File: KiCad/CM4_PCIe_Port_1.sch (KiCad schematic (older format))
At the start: 3 parts, among them J14 PCIe_x16

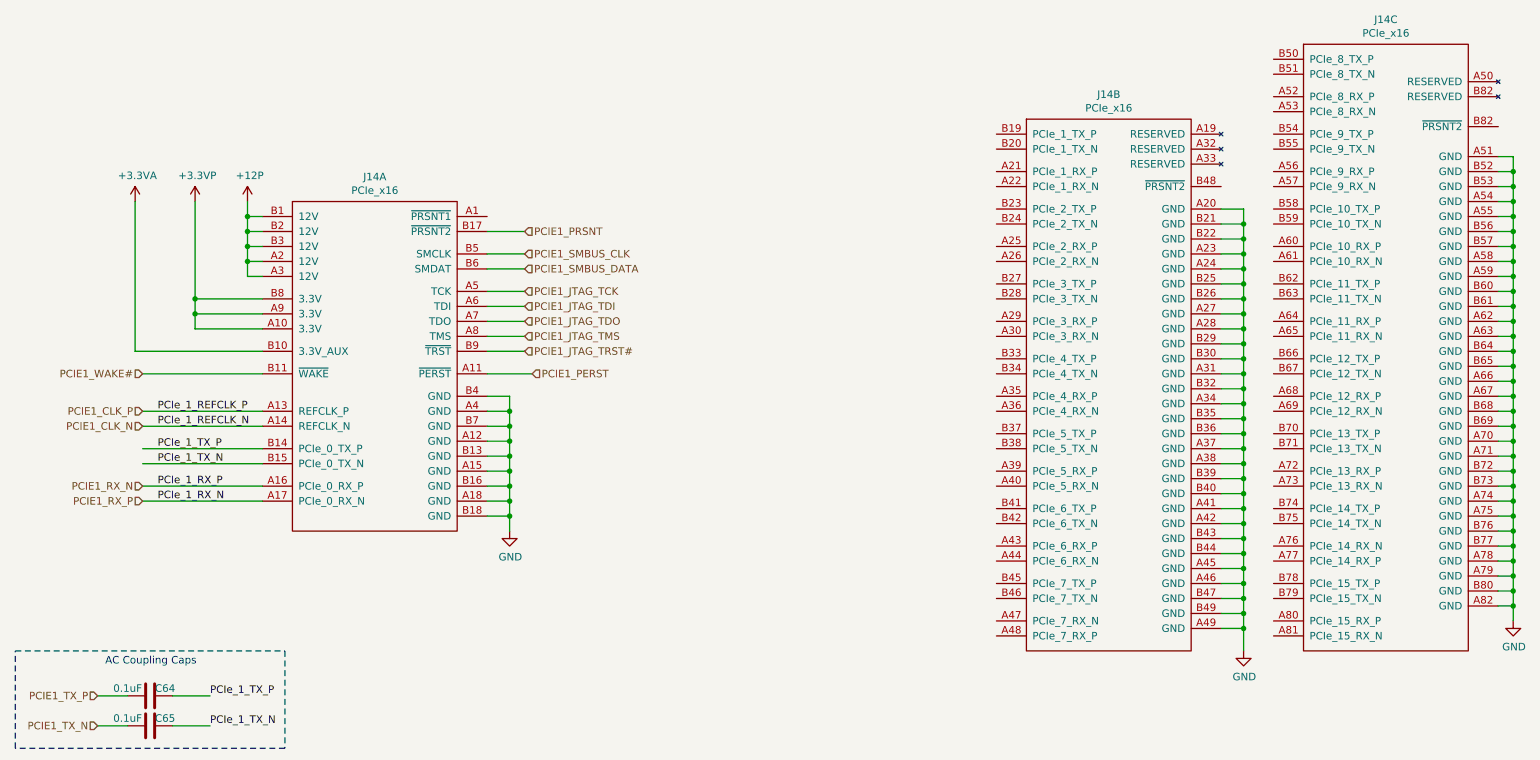
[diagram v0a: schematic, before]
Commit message: Tons of wiring and pin straps for PCI-e Switch
Also re-did some hierarchical labels for JTAG
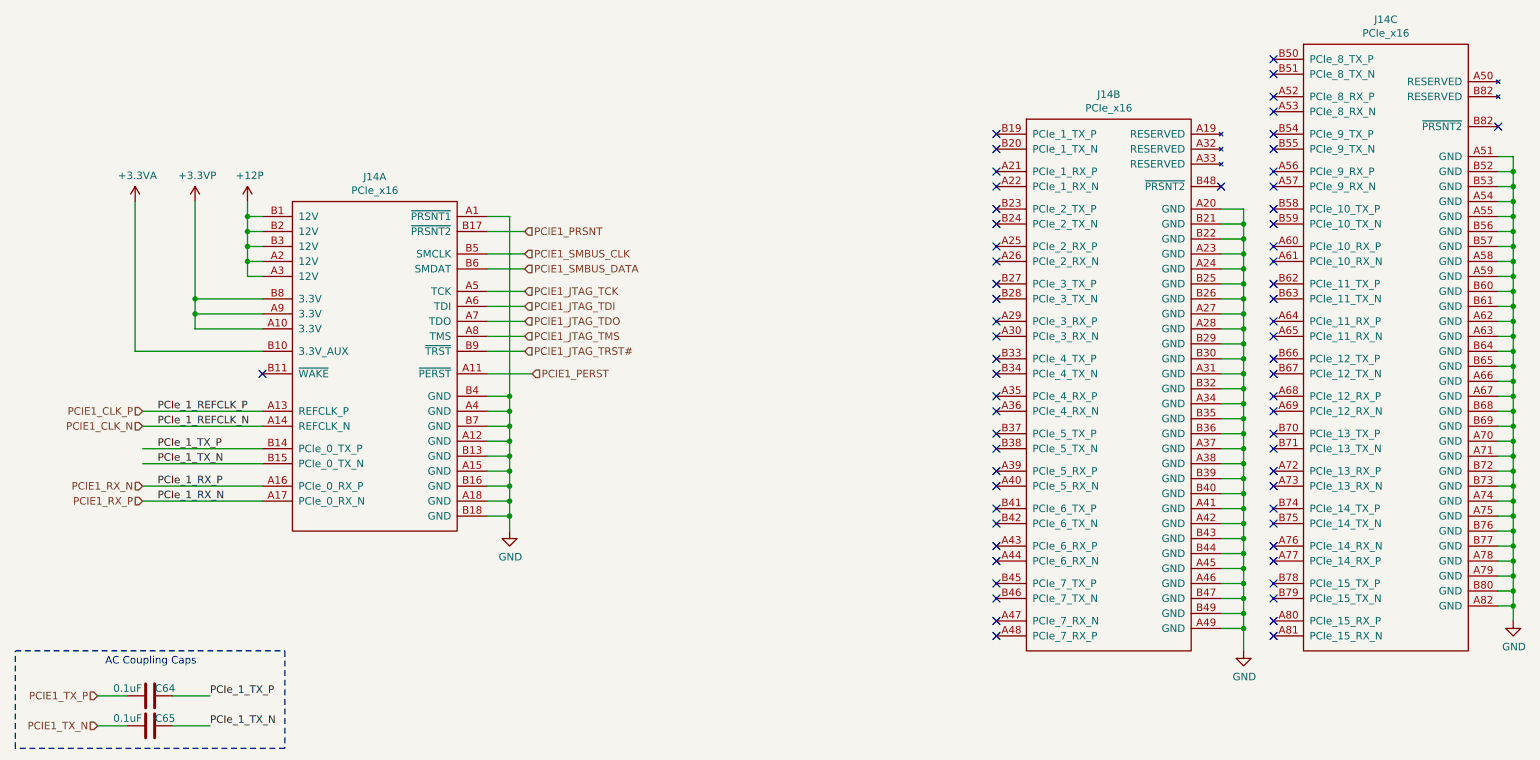
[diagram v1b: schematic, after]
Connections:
- net GND: now also J14.A1 (~PRSNT1)
- net PCIE1_WAKE#: no longer names the net of J14.B11 (~WAKE)
- no-connect marks 0 -> 63
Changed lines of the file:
@@
-$Comp
-L CM4_MATX:PCIe_x16 J14
-U 1 1 5FECC3A6
-P 3450 4600
-AR Path="/5FCA7683/5FECC3A6" Ref="J14"  Part="1"
-AR Path="/5FFBC089/5FFBFF2A/5FECC3A6" Ref="J14"  Part="1"
-F 0 "J14" H 3400 6615 50  0000 C CNN
-F 1 "PCIe_x16" H 3400 6524 50  0000 C CNN
-F 2 "CM4_MATX:10018783-10113TLF" H 1650 9000 50  0001 C CNN
-F 3 "" H 1650 9000 50  0001 C CNN
-	1    3450 4600
-	1    0    0    -1
-$EndComp
 $Comp
 L CM4_MATX:PCIe_x16 J14
@@
 F 3 "" H 6500 8450 50  0001 C CNN
 	2    8300 4050
-	1    0    0    -1
-$EndComp
-$Comp
-L CM4_MATX:PCIe_x16 J14
-U 3 1 5FED4A83
-P 10150 3550
-AR Path="/5FCA7683/5FED4A83" Ref="J14"  Part="3"
-AR Path="/5FFBC089/5FFBFF2A/5FED4A83" Ref="J14"  Part="3"
-F 0 "J14" H 10150 5565 50  0000 C CNN
-F 1 "PCIe_x16" H 10150 5474 50  0000 C CNN
-F 2 "CM4_MATX:10018783-10113TLF" H 8350 7950 50  0001 C CNN
-F 3 "" H 8350 7950 50  0001 C CNN
-	3    10150 3550
 	1    0    0    -1
 $EndComp
@@
 PCIE1_SMBUS_DATA
 Wire Wire Line
-	2650 3900 1850 3900
-Text HLabel 1850 3900 0    50   Input ~ 0
-PCIE1_WAKE#
-Wire Wire Line
 	4150 3350 4400 3350
 Wire Wire Line
@@
 Text HLabel 4400 3750 2    50   Input ~ 0
 PCIE1_JTAG_TRST#
+NoConn ~ 7550 2300
+NoConn ~ 7550 2550
+NoConn ~ 7550 2400
+NoConn ~ 7550 2650
+NoConn ~ 7550 2800
+NoConn ~ 7550 2900
+NoConn ~ 7550 3050
+NoConn ~ 7550 3150
+NoConn ~ 7550 3300
+NoConn ~ 7550 3400
+NoConn ~ 7550 3550
+NoConn ~ 7550 3650
+NoConn ~ 7550 3800
+NoConn ~ 7550 3900
+NoConn ~ 7550 4050
+NoConn ~ 7550 4150
+NoConn ~ 7550 4300
+NoConn ~ 7550 4400
+NoConn ~ 7550 4550
+NoConn ~ 7550 4650
+NoConn ~ 7550 4800
+NoConn ~ 7550 4900
+NoConn ~ 7550 5050
+NoConn ~ 7550 5150
+NoConn ~ 7550 5300
+NoConn ~ 7550 5400
+NoConn ~ 7550 5550
+NoConn ~ 7550 5650
+NoConn ~ 9050 2650
+NoConn ~ 10900 2250
+NoConn ~ 9400 1900
+NoConn ~ 9400 1800
+NoConn ~ 9400 2150
+$Comp
+L CM4_MATX:PCIe_x16 J14
+U 3 1 5FED4A83
+P 10150 3550
+AR Path="/5FCA7683/5FED4A83" Ref="J14"  Part="3"
+AR Path="/5FFBC089/5FFBFF2A/5FED4A83" Ref="J14"  Part="3"
+F 0 "J14" H 10150 5565 50  0000 C CNN
+F 1 "PCIe_x16" H 10150 5474 50  0000 C CNN
+F 2 "CM4_MATX:10018783-10113TLF" H 8350 7950 50  0001 C CNN
+F 3 "" H 8350 7950 50  0001 C CNN
+	3    10150 3550
+	1    0    0    -1
+$EndComp
+NoConn ~ 9400 2050
+NoConn ~ 9400 2300
+NoConn ~ 9400 2400
+NoConn ~ 9400 2550
+NoConn ~ 9400 2650
+NoConn ~ 9400 2800
+NoConn ~ 9400 2900
+NoConn ~ 9400 3050
+NoConn ~ 9400 3150
+NoConn ~ 9400 3300
+NoConn ~ 9400 3400
+NoConn ~ 9400 3550
+NoConn ~ 9400 3650
+NoConn ~ 9400 3800
+NoConn ~ 9400 3900
+NoConn ~ 9400 4050
+NoConn ~ 9400 4150
+NoConn ~ 9400 4300
+NoConn ~ 9400 4400
+NoConn ~ 9400 4550
+NoConn ~ 9400 4650
+NoConn ~ 9400 4800
+NoConn ~ 9400 4900
+NoConn ~ 9400 5050
+NoConn ~ 9400 5150
+NoConn ~ 9400 5300
+NoConn ~ 9400 5400
+NoConn ~ 9400 5550
+NoConn ~ 9400 5650
+$Comp
+L CM4_MATX:PCIe_x16 J14
+U 1 1 5FECC3A6
+P 3450 4600
+AR Path="/5FCA7683/5FECC3A6" Ref="J14"  Part="1"
+AR Path="/5FFBC089/5FFBFF2A/5FECC3A6" Ref="J14"  Part="1"
+F 0 "J14" H 3400 6615 50  0000 C CNN
+F 1 "PCIe_x16" H 3400 6524 50  0000 C CNN
+F 2 "CM4_MATX:10018783-10113TLF" H 1650 9000 50  0001 C CNN
+F 3 "" H 1650 9000 50  0001 C CNN
+	1    3450 4600
+	1    0    0    -1
+$EndComp
+Wire Wire Line
+	4150 2850 4300 2850
+Wire Wire Line
+	4300 2850 4300 4050
+Connection ~ 4300 4050
+NoConn ~ 2650 3900
 $EndSCHEMATC

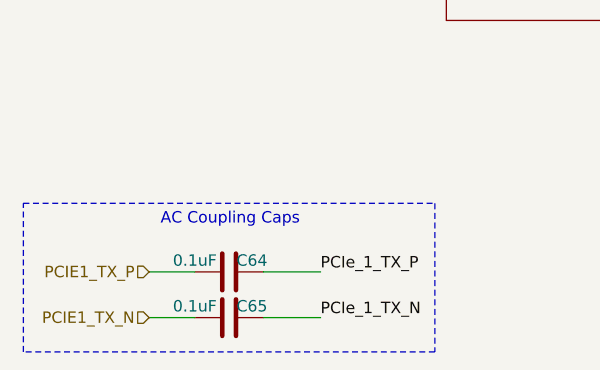
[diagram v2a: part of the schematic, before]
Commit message: Started picking passive components, overhauled library
Cleaned up a bunch of schematic library references.
Added datasheets, descriptions for a lot of existing parts.
Picked most capacitor parts, still a couple left.
Cleaned up a fair few footprint references.
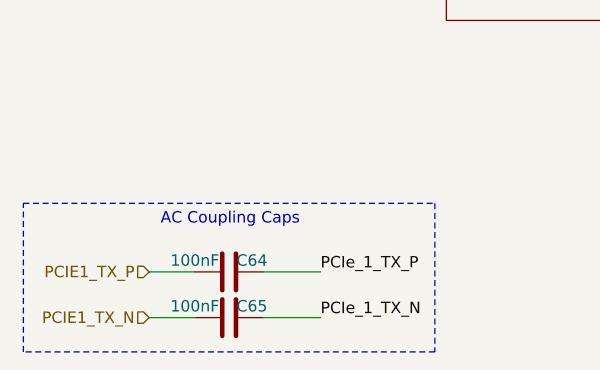
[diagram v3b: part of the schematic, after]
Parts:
- C64, C65: value 0.1uF -> 100nF; footprint (none) -> CM4_MATX:C_0402_1005Metric_Pad0.74x0.62mm_HandSolder; Description (none) -> 10V 0.1uF X5R 0402 20% Tol; Mfr. (none) -> AVX; Mfr. No (none) -> 0402ZD104MAT4A; Mouser Part Number (none) -> 581-0402ZD104MAT4A; Mouser Price/Stock (none) -> https://www.mouser.co.uk/ProductDetail/AVX/0402ZD104MAT4A/?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
- J14: Description (none) -> Amphenol FCI PCI-e x16 Connector 164 POS; Mfr. (none) -> Amphenol; Mfr. No (none) -> 10018783-10113TLF; Mouser Part Number (none) -> 649-18783-10113TLF; Mouser Price/Stock (none) -> https://www.mouser.co.uk/ProductDetail/Amphenol-FCI/1001878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
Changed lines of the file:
@@
 $Descr A4 11693 8268
 encoding utf-8
-Sheet 12 16
+Sheet 15 16
 Title "PCIe x16 - Slot 1"
 Date "2021-02-08"
@@
 PCIE1_RX_P
 $Comp
-L power:GND #PWR0142
+L CM4_MATX:GND #PWR0142
 U 1 1 5FE8F6A6
 P 4300 4950
@@
 PCIe_1_RX_N
 $Comp
-L power:+12P #PWR0143
+L CM4_MATX:+12P #PWR0143
 U 1 1 5FE94417
 P 2550 2750
@@
 	2650 2850 2550 2850
 $Comp
-L power:+3.3VP #PWR0145
+L CM4_MATX:+3.3VP #PWR0145
 U 1 1 5FE971A3
 P 2200 2750
@@
 	2650 3400 2200 3400
 $Comp
-L power:+3.3VA #PWR0184
+L CM4_MATX:+3.3VA #PWR0184
 U 1 1 5FE9A251
 P 1800 2750
@@
 F 1 "PCIe_x16" H 8300 5974 50  0000 C CNN
 F 2 "CM4_MATX:10018783-10113TLF" H 6500 8450 50  0001 C CNN
-F 3 "" H 6500 8450 50  0001 C CNN
+F 3 "https://www.amphenol-icc.com/media/wysiwyg/files/documentation/datasheet/ssio/ssio_pcie_gen3.pdf" H 6500 8450 50  0001 C CNN
+F 4 "Amphenol FCI PCI-e x16 Connector 164 POS" H 8300 4050 50  0001 C CNN "Description"
+F 5 "649-18783-10113TLF" H 8300 4050 50  0001 C CNN "Mouser Part Number"
+F 6 "https://www.mouser.co.uk/ProductDetail/Amphenol-FCI/10018783-10113TLF/?qs=%2Fha2pyFadugRWVTwF3IyzEudyJIuC5mu1uxWW1BR%252B5VORiWMhxM3Zw%3D%3D" H 8300 4050 50  0001 C CNN "Mouser Price/Stock"
+F 7 "Amphenol" H 8300 4050 50  0001 C CNN "Mfr."
+F 8 "10018783-10113TLF" H 8300 4050 50  0001 C CNN "Mfr. No"
 	2    8300 4050
 	1    0    0    -1
@@
 	11000 2550 11000 2650
 $Comp
-L power:GND #PWR0191
+L CM4_MATX:GND #PWR0191
 U 1 1 6000497C
 P 9200 5750
@@
 $EndComp
 $Comp
-L power:GND #PWR0192
+L CM4_MATX:GND #PWR0192
 U 1 1 60004C75
 P 11000 5550
@@
 AR Path="/5FFBC089/5FFBFF2A/5FEEAFF2" Ref="C65"  Part="1"
 F 0 "C65" V 1850 6350 50  0000 C CNN
-F 1 "0.1uF" V 1850 6100 50  0000 C CNN
-F 2 "" H 1938 6100 50  0001 C CNN
-F 3 "~" H 1900 6250 50  0001 C CNN
+F 1 "100nF" V 1850 6100 50  0000 C CNN
+F 2 "CM4_MATX:C_0402_1005Metric_Pad0.74x0.62mm_HandSolder" H 1938 6100 50  0001 C CNN
+F 3 "https://www.mouser.co.uk/datasheet/2/40/cx5r-776519.pdf" H 1900 6250 50  0001 C CNN
+F 4 "581-0402ZD104MAT4A" H 1900 6250 50  0001 C CNN "Mouser Part Number"
+F 5 "https://www.mouser.co.uk/ProductDetail/AVX/0402ZD104MAT4A/?qs=sGAEpiMZZMvsSlwiRhF8qud6rLLpfNdE%2FYSoyEGdkn4%3D" H 1900 6250 50  0001 C CNN "Mouser Price/Stock"
+F 6 "AVX" H 1900 6250 50  0001 C CNN "Mfr."
+F 7 "0402ZD104MAT4A" H 1900 6250 50  0001 C CNN "Mfr. No"
+F 8 "10V 0.1uF X5R 0402 20% Tol" H 1900 6250 50  0001 C CNN "Description"
 	1    1900 6250
 	0    1    1    0
@@
 AR Path="/5FFBC089/5FFBFF2A/5FEEB402" Ref="C64"  Part="1"
 F 0 "C64" V 1950 5950 50  0000 C CNN
-F 1 "0.1uF" V 1950 6200 50  0000 C CNN
-F 2 "" H 1938 5900 50  0001 C CNN
-F 3 "~" H 1900 6050 50  0001 C CNN
+F 1 "100nF" V 1950 6200 50  0000 C CNN
+F 2 "CM4_MATX:C_0402_1005Metric_Pad0.74x0.62mm_HandSolder" H 1938 5900 50  0001 C CNN
+F 3 "https://www.mouser.co.uk/datasheet/2/40/cx5r-776519.pdf" H 1900 6050 50  0001 C CNN
+F 4 "581-0402ZD104MAT4A" H 1900 6050 50  0001 C CNN "Mouser Part Number"
+F 5 "https://www.mouser.co.uk/ProductDetail/AVX/0402ZD104MAT4A/?qs=sGAEpiMZZMvsSlwiRhF8qud6rLLpfNdE%2FYSoyEGdkn4%3D" H 1900 6050 50  0001 C CNN "Mouser Price/Stock"
+F 6 "AVX" H 1900 6050 50  0001 C CNN "Mfr."
+F 7 "0402ZD104MAT4A" H 1900 6050 50  0001 C CNN "Mfr. No"
+F 8 "10V 0.1uF X5R 0402 20% Tol" H 1900 6050 50  0001 C CNN "Description"
 	1    1900 6050
 	0    -1   -1   0
@@
 F 1 "PCIe_x16" H 10150 5474 50  0000 C CNN
 F 2 "CM4_MATX:10018783-10113TLF" H 8350 7950 50  0001 C CNN
-F 3 "" H 8350 7950 50  0001 C CNN
+F 3 "https://www.amphenol-icc.com/media/wysiwyg/files/documentation/datasheet/ssio/ssio_pcie_gen3.pdf" H 8350 7950 50  0001 C CNN
+F 4 "Amphenol FCI PCI-e x16 Connector 164 POS" H 10150 3550 50  0001 C CNN "Description"
+F 5 "649-18783-10113TLF" H 10150 3550 50  0001 C CNN "Mouser Part Number"
+F 6 "https://www.mouser.co.uk/ProductDetail/Amphenol-FCI/10018783-10113TLF/?qs=%2Fha2pyFadugRWVTwF3IyzEudyJIuC5mu1uxWW1BR%252B5VORiWMhxM3Zw%3D%3D" H 10150 3550 50  0001 C CNN "Mouser Price/Stock"
+F 7 "Amphenol" H 10150 3550 50  0001 C CNN "Mfr."
+F 8 "10018783-10113TLF" H 10150 3550 50  0001 C CNN "Mfr. No"
 	3    10150 3550
 	1    0    0    -1
@@
 F 1 "PCIe_x16" H 3400 6524 50  0000 C CNN
 F 2 "CM4_MATX:10018783-10113TLF" H 1650 9000 50  0001 C CNN
-F 3 "" H 1650 9000 50  0001 C CNN
+F 3 "https://www.amphenol-icc.com/media/wysiwyg/files/documentation/datasheet/ssio/ssio_pcie_gen3.pdf" H 1650 9000 50  0001 C CNN
+F 4 "Amphenol FCI PCI-e x16 Connector 164 POS" H 3450 4600 50  0001 C CNN "Description"
+F 5 "649-18783-10113TLF" H 3450 4600 50  0001 C CNN "Mouser Part Number"
+F 6 "https://www.mouser.co.uk/ProductDetail/Amphenol-FCI/10018783-10113TLF/?qs=%2Fha2pyFadugRWVTwF3IyzEudyJIuC5mu1uxWW1BR%252B5VORiWMhxM3Zw%3D%3D" H 3450 4600 50  0001 C CNN "Mouser Price/Stock"
+F 7 "Amphenol" H 3450 4600 50  0001 C CNN "Mfr."
+F 8 "10018783-10113TLF" H 3450 4600 50  0001 C CNN "Mfr. No"
 	1    3450 4600
 	1    0    0    -1

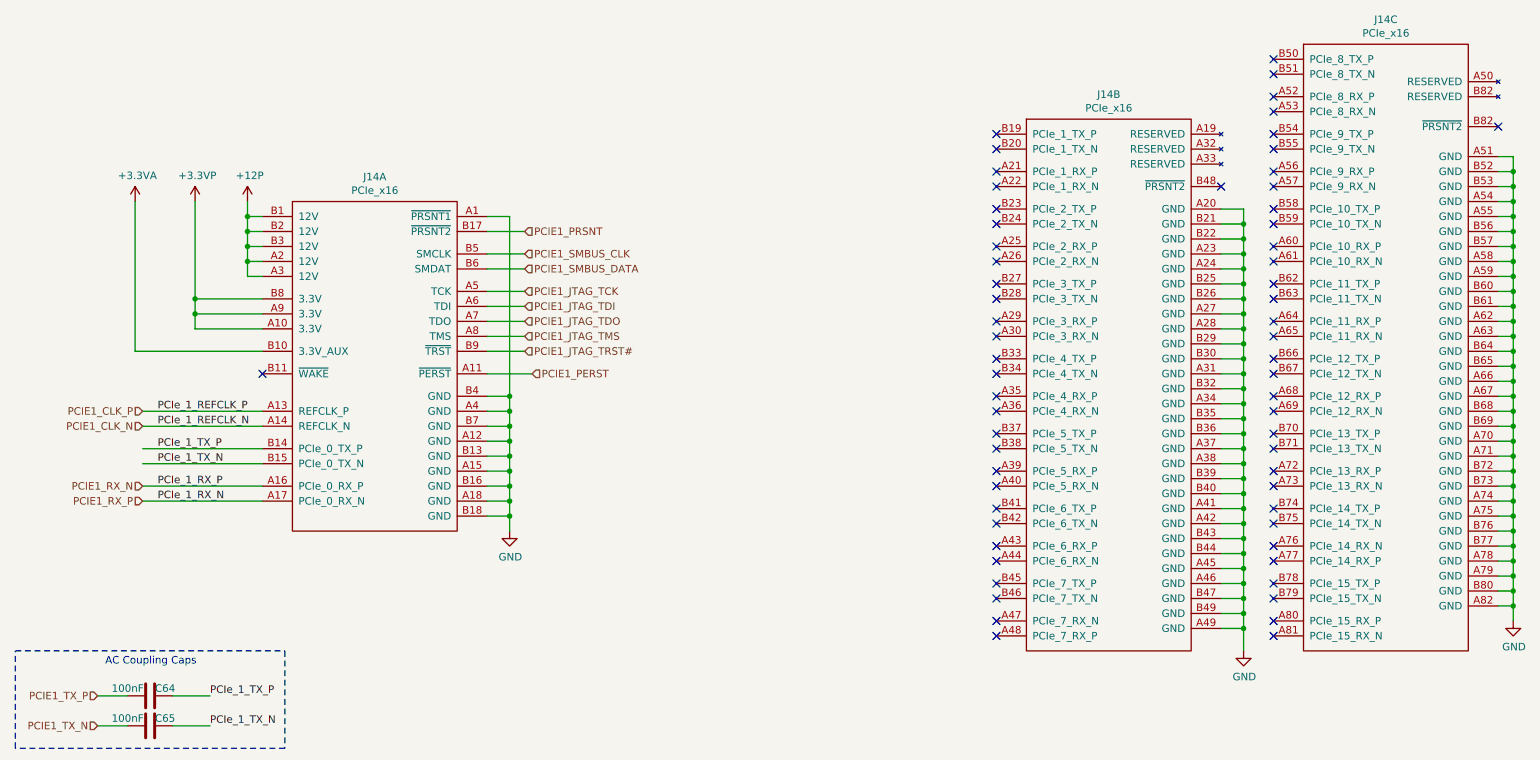
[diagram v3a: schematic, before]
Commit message: Imported new components to the PCB and moved some components
Updated PDFs and added two new board layers. One for ground and a second for power (voltage to be decided)
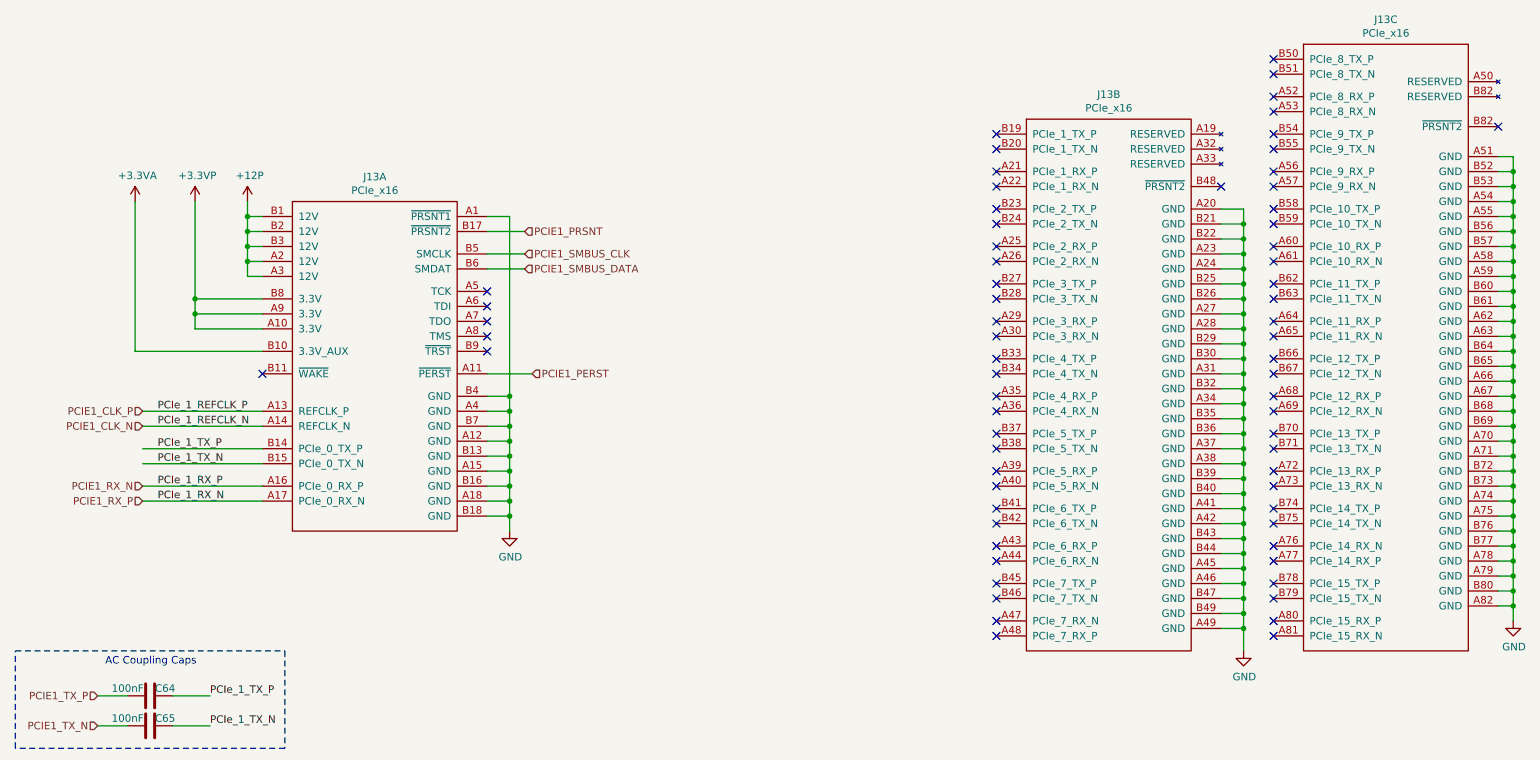
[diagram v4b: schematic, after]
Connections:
- net PCIE1_JTAG_TCK: no longer names the net of J14.A5 (TCK)
- net PCIE1_JTAG_TDI: no longer names the net of J14.A6 (TDI)
- net PCIE1_JTAG_TDO: no longer names the net of J14.A7 (TDO)
- net PCIE1_JTAG_TMS: no longer names the net of J14.A8 (TMS)
- net PCIE1_JTAG_TRST#: no longer names the net of J14.B9 (~TRST)
- no-connect marks 63 -> 68
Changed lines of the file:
@@
 $Descr A4 11693 8268
 encoding utf-8
-Sheet 15 16
+Sheet 14 15
 Title "PCIe x16 - Slot 1"
 Date "2021-02-08"
@@
 P 8300 4050
 AR Path="/5FCA7683/5FED16BC" Ref="J14"  Part="2"
-AR Path="/5FFBC089/5FFBFF2A/5FED16BC" Ref="J14"  Part="2"
-F 0 "J14" H 8300 6065 50  0000 C CNN
+AR Path="/5FFBC089/5FFBFF2A/5FED16BC" Ref="J13"  Part="2"
+F 0 "J13" H 8300 6065 50  0000 C CNN
 F 1 "PCIe_x16" H 8300 5974 50  0000 C CNN
 F 2 "CM4_MATX:10018783-10113TLF" H 6500 8450 50  0001 C CNN
@@
 PCIE1_SMBUS_DATA
 Wire Wire Line
-	4150 3350 4400 3350
-Wire Wire Line
-	4150 3450 4400 3450
-Wire Wire Line
-	4150 3550 4400 3550
-Wire Wire Line
-	4150 3650 4400 3650
-Wire Wire Line
-	4150 3750 4400 3750
-Wire Wire Line
 	2550 2850 2550 2750
 Connection ~ 2550 2850
@@
 Wire Wire Line
 	1800 3750 1800 2750
-Text HLabel 4400 3350 2    50   Input ~ 0
-PCIE1_JTAG_TCK
-Text HLabel 4400 3450 2    50   Input ~ 0
-PCIE1_JTAG_TDI
-Text HLabel 4400 3550 2    50   Input ~ 0
-PCIE1_JTAG_TDO
-Text HLabel 4400 3650 2    50   Input ~ 0
-PCIE1_JTAG_TMS
-Text HLabel 4400 3750 2    50   Input ~ 0
-PCIE1_JTAG_TRST#
 NoConn ~ 7550 2300
 NoConn ~ 7550 2550
@@
 P 10150 3550
 AR Path="/5FCA7683/5FED4A83" Ref="J14"  Part="3"
-AR Path="/5FFBC089/5FFBFF2A/5FED4A83" Ref="J14"  Part="3"
-F 0 "J14" H 10150 5565 50  0000 C CNN
+AR Path="/5FFBC089/5FFBFF2A/5FED4A83" Ref="J13"  Part="3"
+F 0 "J13" H 10150 5565 50  0000 C CNN
 F 1 "PCIe_x16" H 10150 5474 50  0000 C CNN
 F 2 "CM4_MATX:10018783-10113TLF" H 8350 7950 50  0001 C CNN
@@
 NoConn ~ 9400 5550
 NoConn ~ 9400 5650
+Wire Wire Line
+	4150 2850 4300 2850
+Wire Wire Line
+	4300 2850 4300 4050
+Connection ~ 4300 4050
+NoConn ~ 2650 3900
 $Comp
 L CM4_MATX:PCIe_x16 J14
@@
 P 3450 4600
 AR Path="/5FCA7683/5FECC3A6" Ref="J14"  Part="1"
-AR Path="/5FFBC089/5FFBFF2A/5FECC3A6" Ref="J14"  Part="1"
-F 0 "J14" H 3400 6615 50  0000 C CNN
+AR Path="/5FFBC089/5FFBFF2A/5FECC3A6" Ref="J13"  Part="1"
+F 0 "J13" H 3400 6615 50  0000 C CNN
 F 1 "PCIe_x16" H 3400 6524 50  0000 C CNN
 F 2 "CM4_MATX:10018783-10113TLF" H 1650 9000 50  0001 C CNN
@@
 	1    0    0    -1
 $EndComp
-Wire Wire Line
-	4150 2850 4300 2850
-Wire Wire Line
-	4300 2850 4300 4050
-Connection ~ 4300 4050
-NoConn ~ 2650 3900
+NoConn ~ 4150 3350
+NoConn ~ 4150 3450
+NoConn ~ 4150 3550
+NoConn ~ 4150 3650
+NoConn ~ 4150 3750
 $EndSCHEMATC
